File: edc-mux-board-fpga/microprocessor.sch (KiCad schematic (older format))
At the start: 1 part, among them U56 SAMD21JXXAM

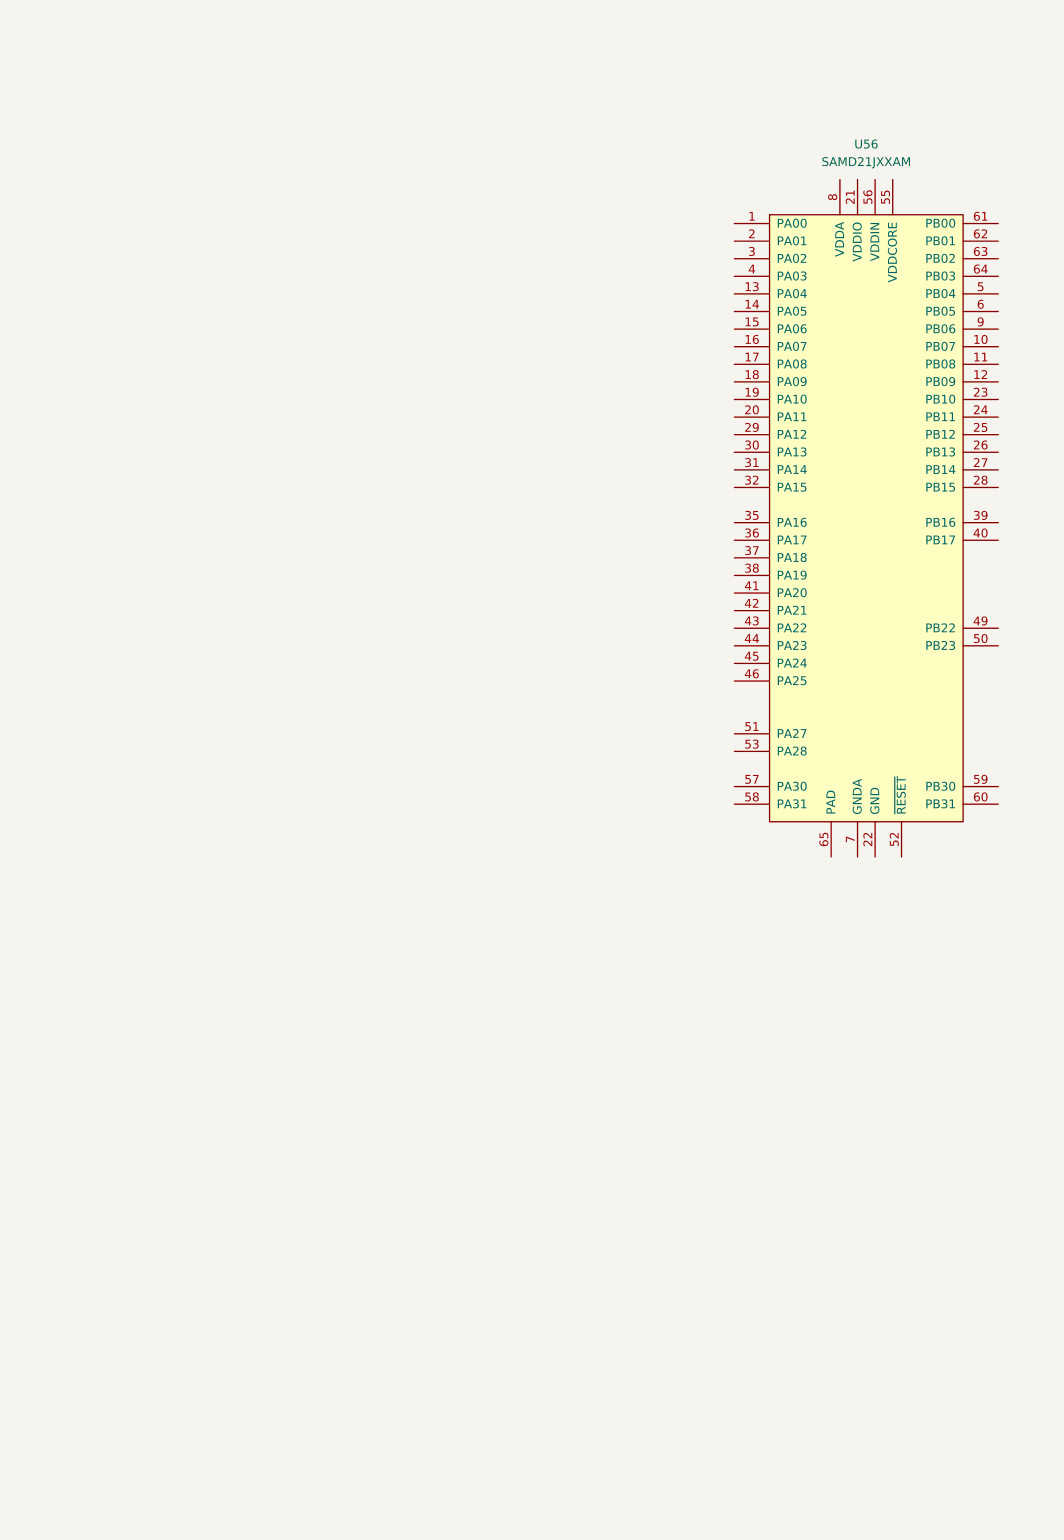
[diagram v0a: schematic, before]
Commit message: power and initial connections for microprocessor
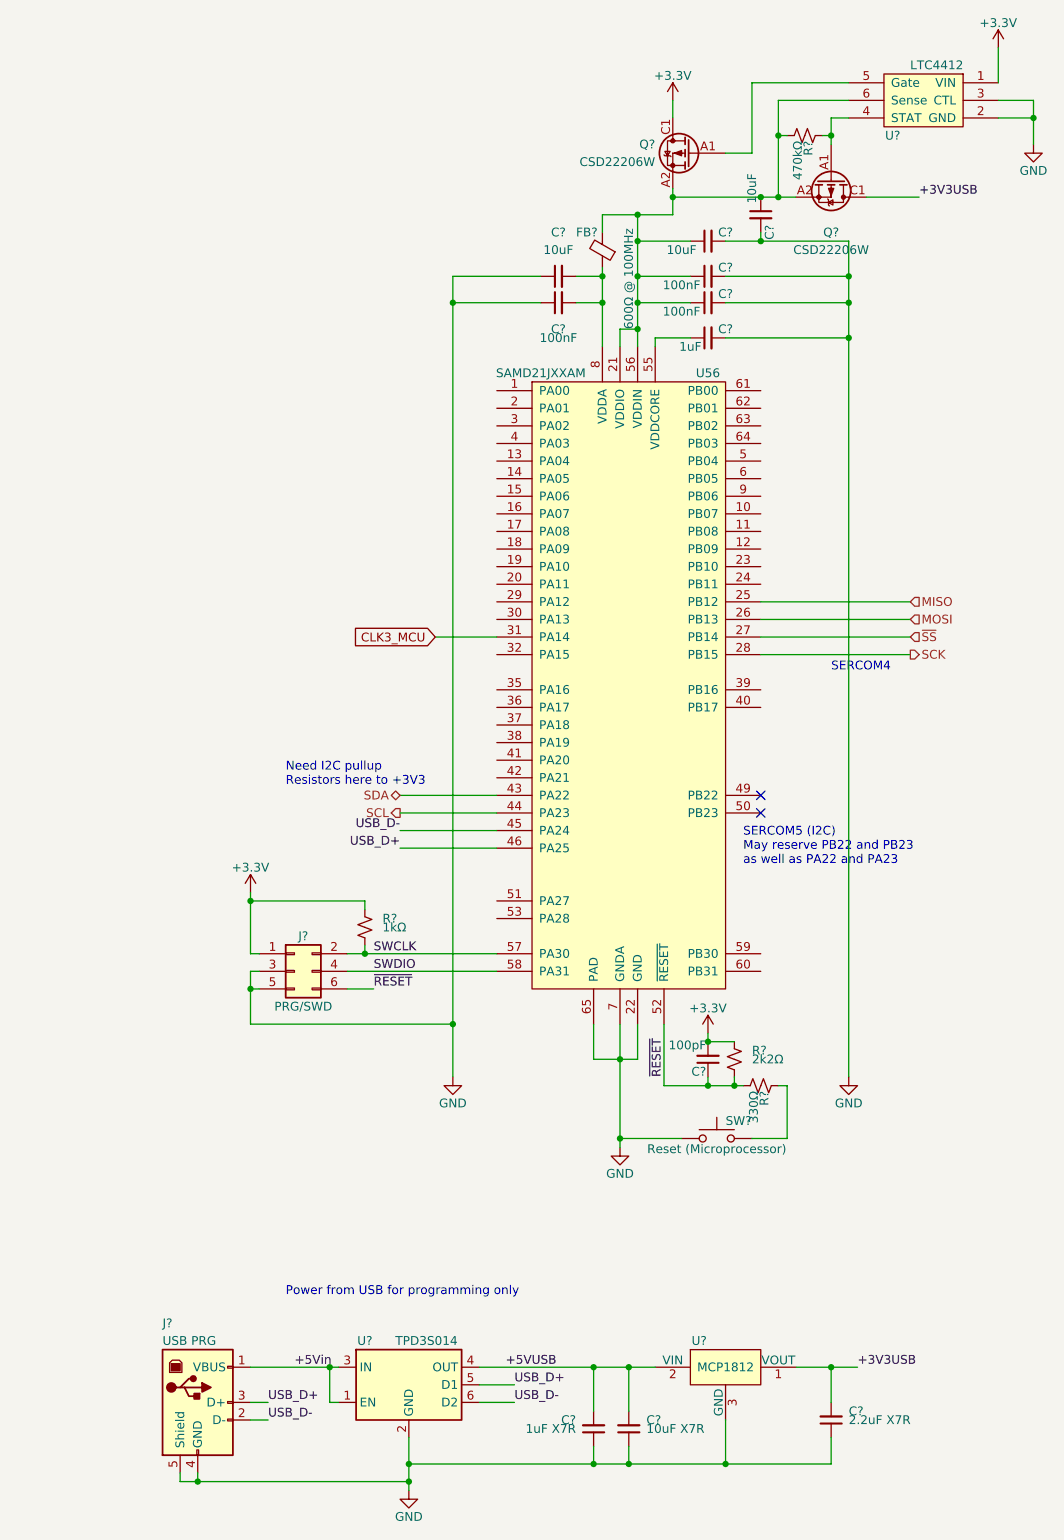
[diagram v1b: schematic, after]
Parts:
- added C? (x3): 10uF, symbol Device:C_Small
- added C? (x3): 100nF, symbol Device:C_Small
- added C?: 100pF, symbol Device:C_Small
- added C?: 1uF, symbol Device:C_Small
- added C?: 1uF X7R, symbol Device:C_Small
- added C?: 2.2uF X7R, symbol Device:C_Small
- added C?: 10uF X7R, symbol Device:C_Small
- added FB?: 600Ω @ 100MHz, Capacitor_SMD:C_0805_2012Metric, symbol Device:Ferrite_Bead_Small
- added J?: PRG/SWD, symbol Connector_Generic:Conn_02x03_Odd_Even
- added J?: USB PRG, symbol Connector:USB_B
- added Q? (x2): CSD22206W, SW-Texas:DSBGA9, symbol SW-Texas:CSD22206W
- added R?: 330Ω, symbol Device:R_Small_US
- added R?: 2k2Ω, symbol Device:R_Small_US
- added R?: 1kΩ, symbol Device:R_Small_US
- added R?: 470kΩ, symbol Device:R_Small_US
- added SW?: Reset (Microprocessor), symbol Switch:SW_Push
- added U?: TPD3S014, Package_TO_SOT_SMD:SOT-23-6, symbol Power_Protection:TPD3S014
- added U?: MCP1812, symbol SW-Microchip:MCP1812
- added U?: LTC4412, Package_TO_SOT_SMD:TSOT-23-6, symbol SW-Linear:LTC4412
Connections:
- net at U56.21 (VDDIO), U56.34 (VDDIO), U56.48 (VDDIO): now also U56.56 (VDDIN), C?.1, C?.1, C?.1, C?.1, FB?.2, Q?.A2 (S), Q?.A2 (S), Q?.A3 (S), Q?.A3 (S), Q?.B1 (S), Q?.B1 (S), Q?.B2 (S), Q?.B2 (S), Q?.B3 (S), Q?.B3 (S), R?.2, U?.6 (Sense)
- net GND: now reaches U56.22 (GND), U56.33 (GND), U56.47 (GND), U56.54 (GND)
- net GND: now also U56.65 (PAD), U56.7 (GNDA), C?.1, C?.1, C?.1, C?.1, C?.1, C?.2, C?.2, C?.2, C?.2, C?.2, J?.3 (Pin_3), J?.4 (GND), J?.5 (Pin_5), J?.5 (Shield), SW?.1, U?.2 (GND), U?.2 (GND), U?.3 (CTL), U?.3 (GND)
- net MISO: now reaches U56.25 (PB12)
- net MOSI: now reaches U56.26 (PB13)
- net ~SS: now reaches U56.27 (PB14)
- net SCK: now reaches U56.28 (PB15)
- net CLK3_MCU: now reaches U56.31 (PA14)
- net SDA: now reaches U56.43 (PA22)
- net SCL: now reaches U56.44 (PA23)
- net USB_D-: now reaches U56.45 (PA24)
- net USB_D-: now also J?.2 (D-), U?.6 (D2)
- net USB_D+: now reaches U56.46 (PA25)
- net USB_D+: now also J?.3 (D+), U?.5 (D1)
- net ~RESET: now reaches U56.52 (~RESET)
- net ~RESET: now also C?.1, J?.6 (Pin_6), R?.1, R?.2
- net at U56.55 (VDDCORE): now also C?.1
- net SWCLK: now reaches U56.57 (PA30)
- net SWCLK: now also J?.2 (Pin_2), R?.1
- net SWDIO: now reaches U56.58 (PA31)
- net SWDIO: now also J?.4 (Pin_4)
- net at U56.8 (VDDA): now also C?.2, C?.2, FB?.1
- new net: R?.1, SW?.2
- new net: Q?.A1 (G), R?.1, U?.4 (STAT)
- new net: Q?.A1 (G), U?.5 (Gate)
- new net +3V3: C?.2, J?.1 (Pin_1), Q?.C1 (D), Q?.C2 (D), Q?.C3 (D), R?.2, R?.2, U?.1 (VIN)
- new net +3V3USB: C?.2, Q?.C1 (D), Q?.C2 (D), Q?.C3 (D), U?.1 (VOUT)
- new net +5VUSB: C?.2, C?.2, U?.2 (VIN), U?.4 (OUT)
- new net +5Vin: J?.1 (VBUS), U?.1 (EN), U?.3 (IN)
- no-connect marks 0 -> 2
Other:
- note added: "Need I2C pullup\nResistors here to +3V3"
- note added: "Power from USB for programming only"
- note added: "SERCOM4"
- note added: "SERCOM5 (I2C)\nMay reserve PB22 and PB23\nas well as PA22 and PA23"
- moved on the sheet: U56

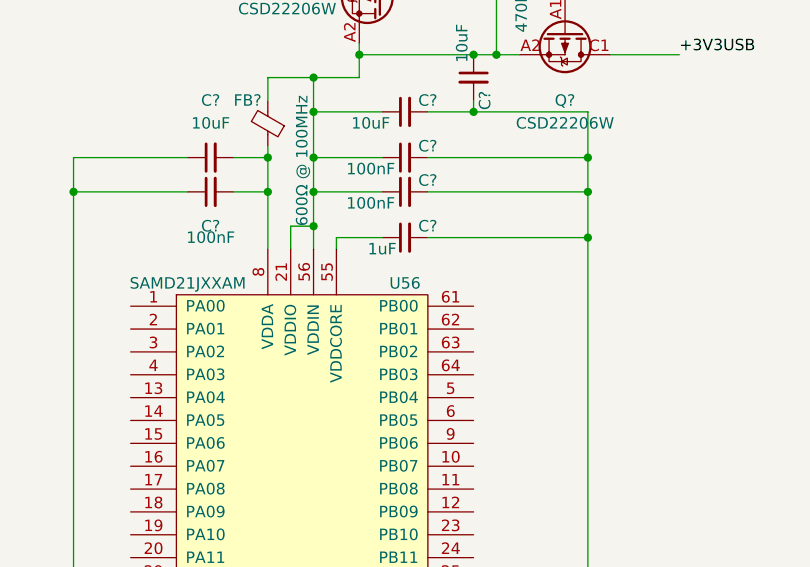
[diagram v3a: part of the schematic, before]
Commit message: unannotated components after major changes
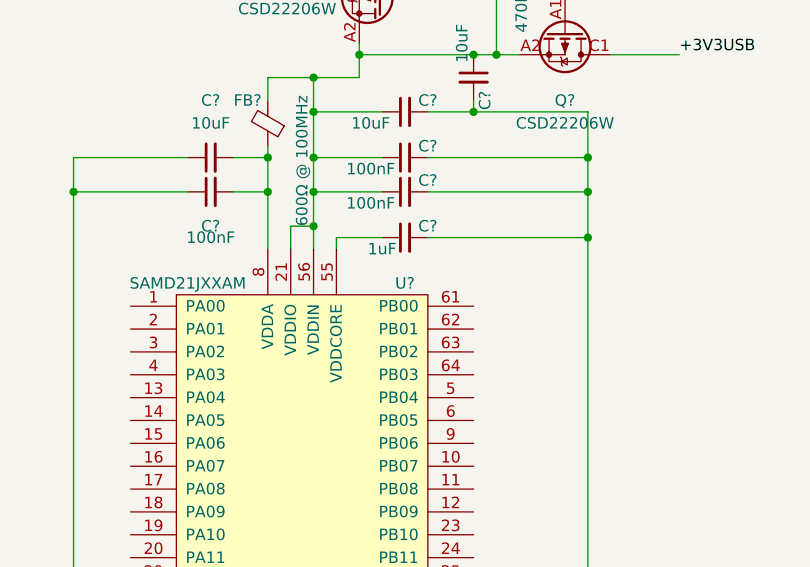
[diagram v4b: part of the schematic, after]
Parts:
- renumbered U56 to U?
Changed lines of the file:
@@
 $EndDescr
 $Comp
-L SW-Microchip:SAMD21JXXAM U56
+L SW-Microchip:SAMD21JXXAM U?
 U 1 1 5CB265DB
 P 4300 4400
-F 0 "U56" H 4750 6100 50  0000 C CNN
+F 0 "U?" H 4750 6100 50  0000 C CNN
 F 1 "SAMD21JXXAM" H 3800 6100 50  0000 C CNN
 F 2 "Package_DFN_QFN:QFN-64-1EP_9x9mm_P0.5mm_EP4.7x4.7mm_ThermalVias" H 3100 6950 50  0001 C CNN

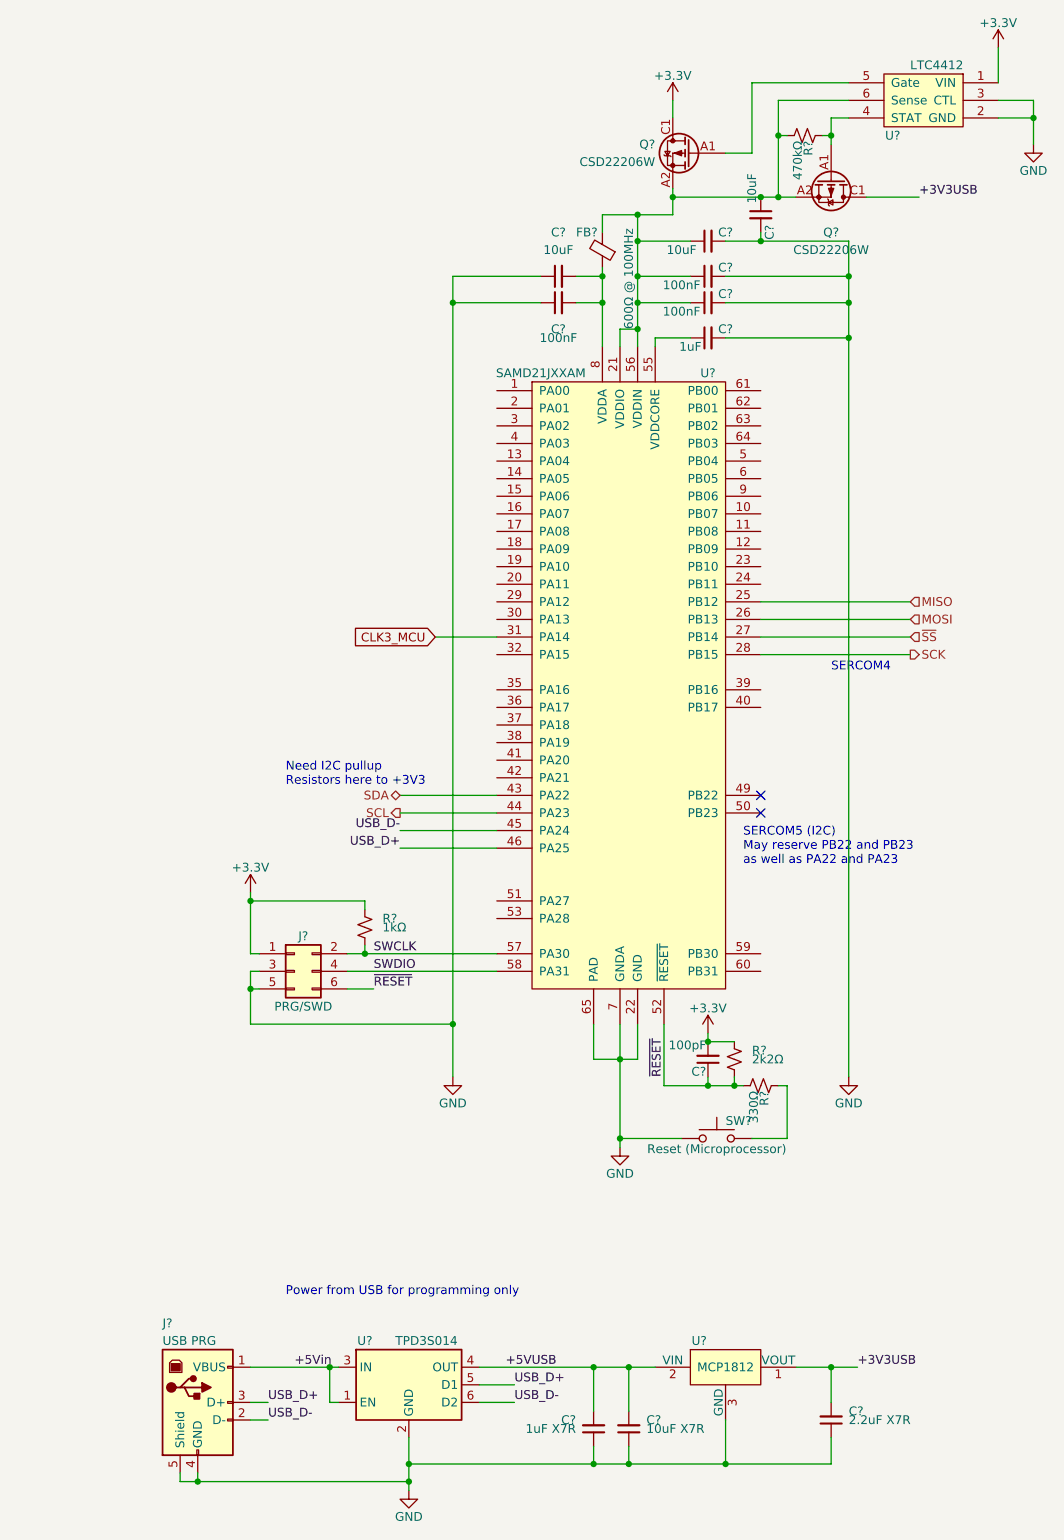
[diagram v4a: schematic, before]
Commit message: Finished CODEC and MCU interconnections
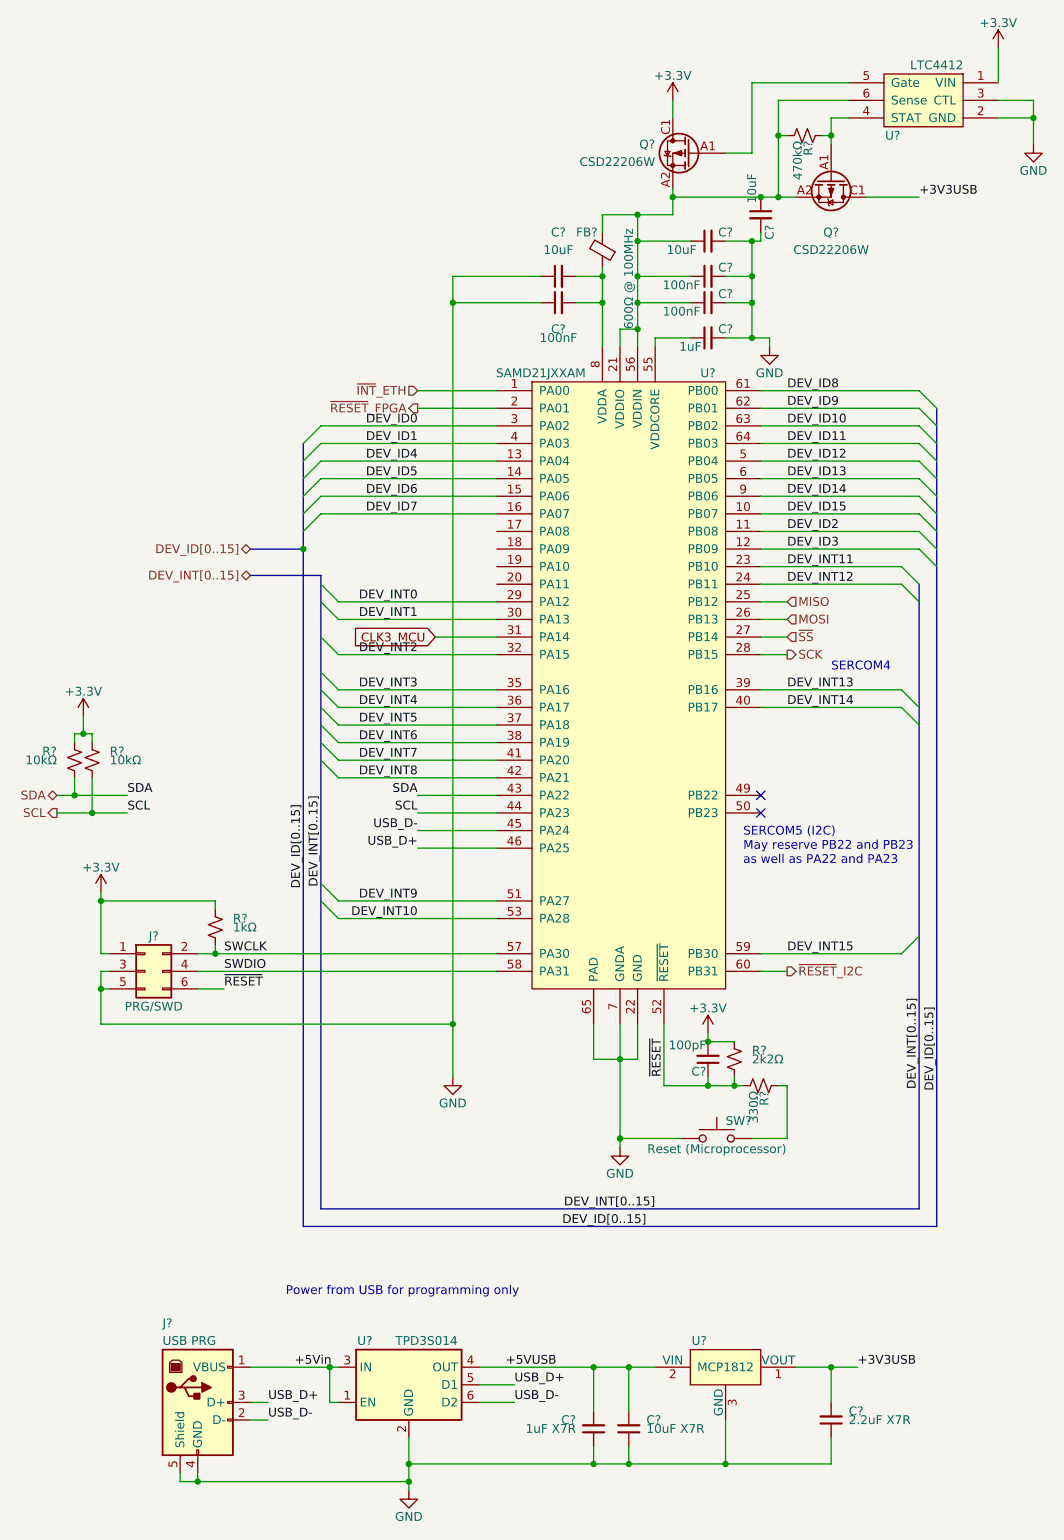
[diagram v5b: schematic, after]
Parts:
- added R? (x2): 10kΩ, symbol Device:R_Small_US
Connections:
- net +3V3: now also R?.2, R?.2
- net SCL: now also R?.1
- net SDA: now also R?.1
- net ~INT~_ETH: now reaches U?.1 (PA00)
- net DEV_ID15: now reaches U?.10 (PB07)
- net DEV_ID2: now reaches U?.11 (PB08)
- net DEV_ID3: now reaches U?.12 (PB09)
- net DEV_ID4: now reaches U?.13 (PA04)
- net DEV_ID5: now reaches U?.14 (PA05)
- net DEV_ID6: now reaches U?.15 (PA06)
- net DEV_ID7: now reaches U?.16 (PA07)
- net ~RESET~_FPGA: now reaches U?.2 (PA01)
- net DEV_INT11: now reaches U?.23 (PB10)
- net DEV_INT12: now reaches U?.24 (PB11)
- net DEV_INT0: now reaches U?.29 (PA12)
- net DEV_ID0: now reaches U?.3 (PA02)
- net DEV_INT1: now reaches U?.30 (PA13)
- net DEV_INT2: now reaches U?.32 (PA15)
- net DEV_INT3: now reaches U?.35 (PA16)
- net DEV_INT4: now reaches U?.36 (PA17)
- net DEV_INT5: now reaches U?.37 (PA18)
- net DEV_INT6: now reaches U?.38 (PA19)
- net DEV_INT13: now reaches U?.39 (PB16)
- net DEV_ID1: now reaches U?.4 (PA03)
- net DEV_INT14: now reaches U?.40 (PB17)
- net DEV_INT7: now reaches U?.41 (PA20)
- net DEV_INT8: now reaches U?.42 (PA21)
- net DEV_ID12: now reaches U?.5 (PB04)
- net DEV_INT9: now reaches U?.51 (PA27)
- net DEV_INT10: now reaches U?.53 (PA28)
- net DEV_INT15: now reaches U?.59 (PB30)
- net DEV_ID13: now reaches U?.6 (PB05)
- net ~RESET~_I2C: now reaches U?.60 (PB31)
- net DEV_ID8: now reaches U?.61 (PB00)
- net DEV_ID9: now reaches U?.62 (PB01)
- net DEV_ID10: now reaches U?.63 (PB02)
- net DEV_ID11: now reaches U?.64 (PB03)
- net DEV_ID14: now reaches U?.9 (PB06)
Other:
- note removed: "Need I2C pullup\nResistors here to +3V3"
- moved on the sheet: J?, R?
